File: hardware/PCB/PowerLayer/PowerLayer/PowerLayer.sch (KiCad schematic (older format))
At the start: 2 parts, among them J1 Conn_01x03_Female

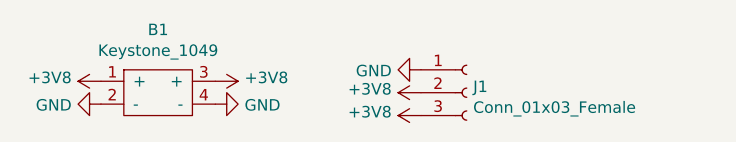
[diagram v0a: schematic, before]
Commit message: Final casing selected and PCB rearranged to fit into the casing
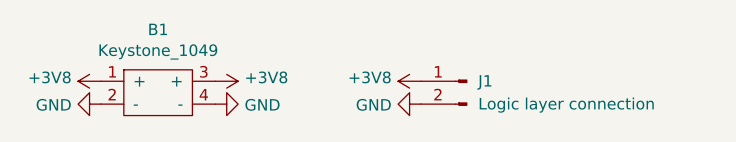
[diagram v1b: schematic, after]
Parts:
- removed J1: Conn_01x03_Female, Connector_PinSocket_2.54mm:PinSocket_1x03_P2.54mm_Vertical, symbol Connector:Conn_01x03_Female
- added J1: Logic layer connection, Connector_PinHeader_2.54mm:PinHeader_1x02_P2.54mm_Vertical, symbol Connector:Conn_01x02_Male
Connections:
- net +3V8: now also J1.1 (Pin_1)
- net GND: now also J1.2 (Pin_2)
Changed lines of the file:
@@
 L power:+3V8 #PWR05
 U 1 1 61A0771B
-P 6900 3450
-F 0 "#PWR05" H 6900 3300 50  0001 C CNN
-F 1 "+3V8" V 6915 3578 50  0000 L CNN
-F 2 "" H 6900 3450 50  0001 C CNN
-F 3 "" H 6900 3450 50  0001 C CNN
-	1    6900 3450
+P 6900 3400
+F 0 "#PWR05" H 6900 3250 50  0001 C CNN
+F 1 "+3V8" V 6915 3528 50  0000 L CNN
+F 2 "" H 6900 3400 50  0001 C CNN
+F 3 "" H 6900 3400 50  0001 C CNN
+	1    6900 3400
 	0    -1   -1   0
 $EndComp
@@
 $EndComp
 $Comp
-L Connector:Conn_01x03_Female J1
-U 1 1 61A27FA9
-P 7100 3450
-F 0 "J1" H 7128 3476 50  0000 L CNN
-F 1 "Conn_01x03_Female" H 7128 3385 50  0000 L CNN
-F 2 "Connector_PinSocket_2.54mm:PinSocket_1x03_P2.54mm_Vertical" H 7100 3450 50  0001 C CNN
-F 3 "~" H 7100 3450 50  0001 C CNN
-	1    7100 3450
-	1    0    0    -1
-$EndComp
-$Comp
 L power:GND #PWR06
 U 1 1 61A07B60
-P 6900 3350
-F 0 "#PWR06" H 6900 3100 50  0001 C CNN
-F 1 "GND" V 6905 3222 50  0000 R CNN
-F 2 "" H 6900 3350 50  0001 C CNN
-F 3 "" H 6900 3350 50  0001 C CNN
-	1    6900 3350
+P 6900 3500
+F 0 "#PWR06" H 6900 3250 50  0001 C CNN
+F 1 "GND" V 6905 3372 50  0000 R CNN
+F 2 "" H 6900 3500 50  0001 C CNN
+F 3 "" H 6900 3500 50  0001 C CNN
+	1    6900 3500
 	0    1    1    0
 $EndComp
 $Comp
-L power:+3V8 #PWR03
-U 1 1 61A41674
-P 6900 3550
-F 0 "#PWR03" H 6900 3400 50  0001 C CNN
-F 1 "+3V8" V 6915 3678 50  0000 L CNN
-F 2 "" H 6900 3550 50  0001 C CNN
-F 3 "" H 6900 3550 50  0001 C CNN
-	1    6900 3550
-	0    -1   -1   0
+L Connector:Conn_01x02_Male J1
+U 1 1 61B68130
+P 7100 3400
+F 0 "J1" H 7050 3400 50  0000 R CNN
+F 1 "Logic layer connection" H 7050 3300 50  0000 R CNN
+F 2 "Connector_PinHeader_2.54mm:PinHeader_1x02_P2.54mm_Vertical" H 7100 3400 50  0001 C CNN
+F 3 "~" H 7100 3400 50  0001 C CNN
+	1    7100 3400
+	-1   0    0    -1
 $EndComp
 $EndSCHEMATC
